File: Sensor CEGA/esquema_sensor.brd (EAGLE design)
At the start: 69.8 x 73.3 mm, 11 parts

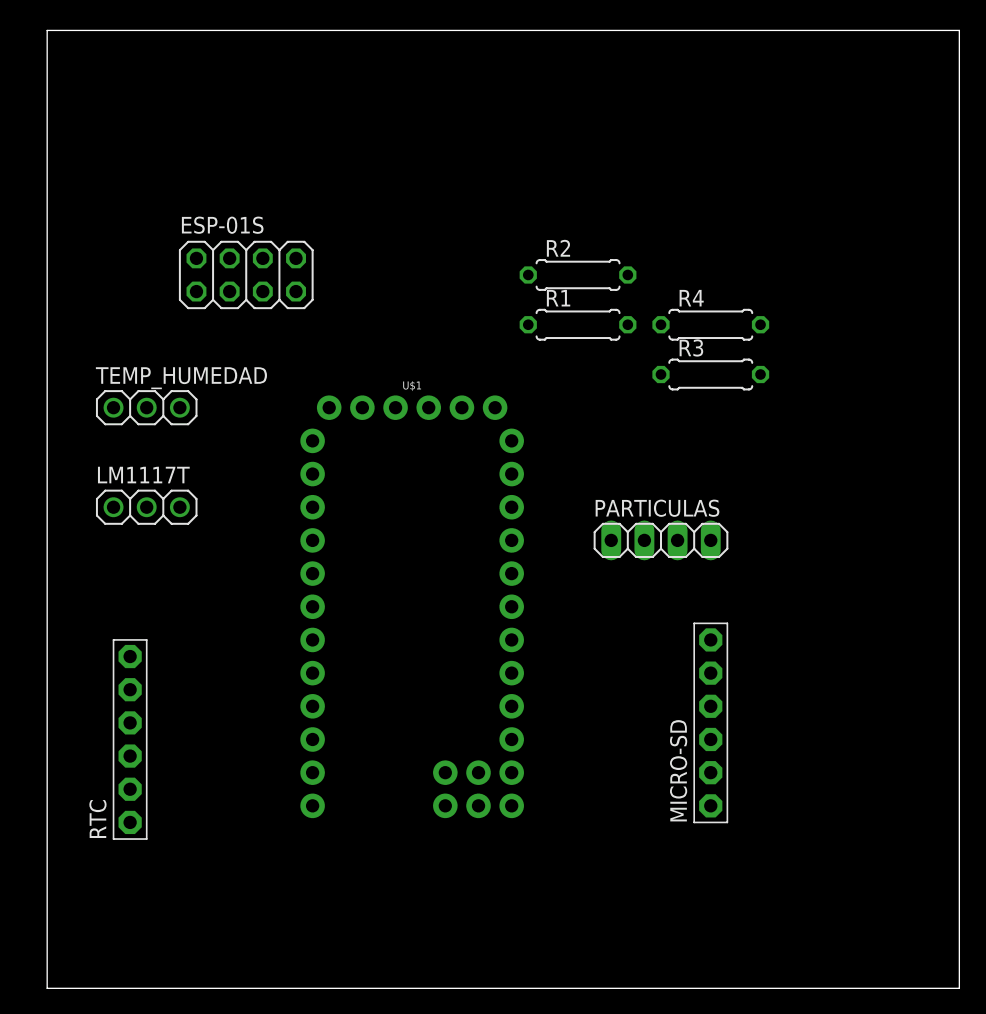
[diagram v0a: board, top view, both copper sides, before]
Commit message: versión 1.0 del sensor en PCB
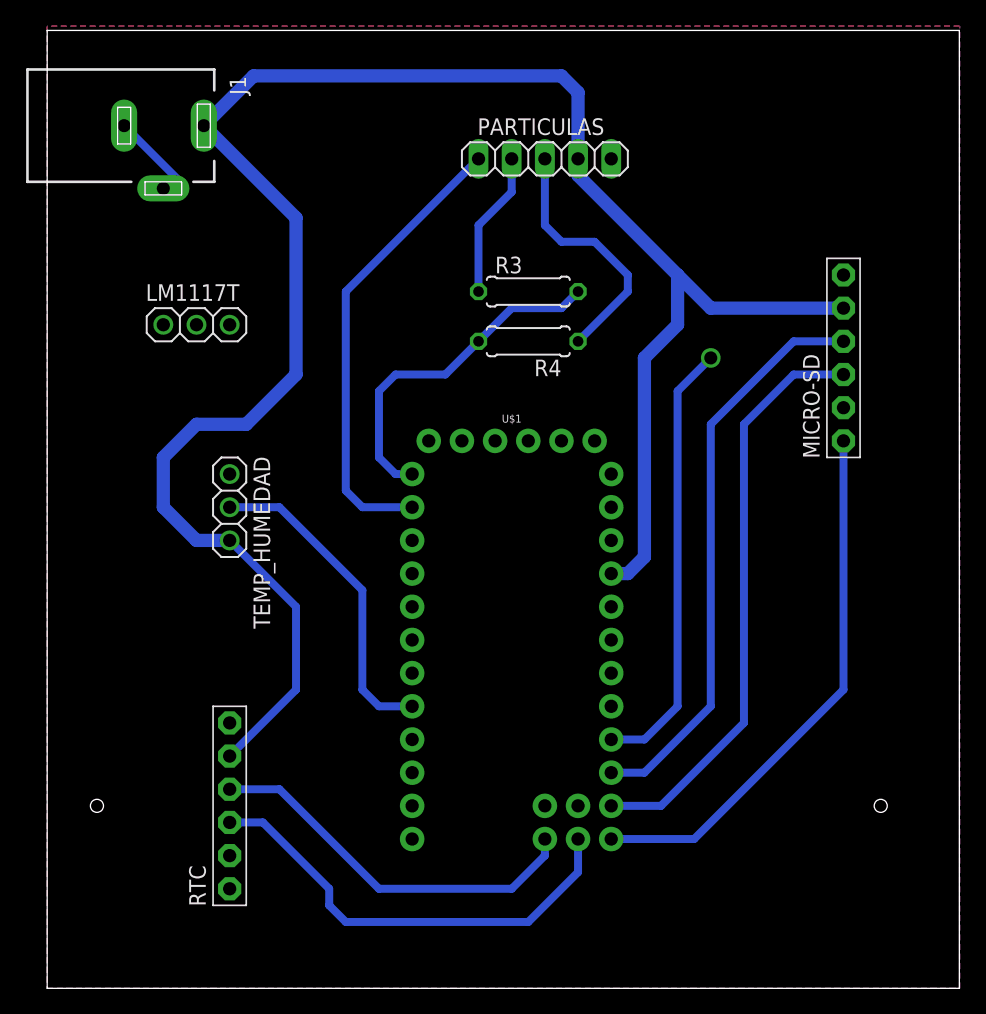
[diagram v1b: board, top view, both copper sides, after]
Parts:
- removed ESP-01S: (no value), pinhead:2X04
- removed R1, R2: (no value), resistor:0207/7
- added J1: DCJ0202, con-jack:DCJ0202
- PARTICULAS: device pinhead:1X04 -> pinhead:1X05
- moved PARTICULAS 30.5 mm to (38.1, 63.5)
- moved MICRO-SD 29.7 mm to (61.0, 48.3)
- moved R3 15.3 mm to (36.8, 53.3)
- moved LM1117T 14.5 mm to (11.4, 50.8)
- moved R4 14.0 mm to (36.8, 49.5), turned to 180 degrees
- moved TEMP_HUMEDAD 9.92 mm to (14.0, 36.8), turned to 270 degrees
- moved RTC 9.16 mm to (14.0, 14.0)
- moved U$1 8.03 mm to (35.6, 26.7)
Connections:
- removed net GND: U$1.23
- removed net N$4: ESP-01S.2, R1.2, R2.2
- net +3V3: no longer ESP-01S.1, ESP-01S.5
- net +5V: now also J1.1
- net GNDA: now also J1.2, J1.3, U$1.23; no longer ESP-01S.8, R2.1
- net N$1: no longer R1.1
- net N$3: no longer ESP-01S.7
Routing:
- net +5V: track 0.00 -> 161.7 mm
- net N$11: track 0.00 -> 44.8 mm
- net N$10: track 0.00 -> 44.1 mm
- net N$13: track 0.00 -> 41.6 mm
- net N$5: track 0.00 -> 35.2 mm
- net A5: track 0.00 -> 34.7 mm
- net N$12: track 0.00 -> 33.9 mm, vias 0 -> 1
- net A4: track 0.00 -> 29.6 mm
- net GNDA: track 0.00 -> 26.8 mm
- net N$6: track 0.00 -> 26.5 mm
- net N$8: track 0.00 -> 24.7 mm
- net N$7: track 0.00 -> 11.2 mm
- added copper zone on layer 1, net GNDA
- added copper zone on layer 16, net GNDA

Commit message: actualizado sensor cega y usain bot
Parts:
- removed LM1117T: (no value), adafruit:1X03
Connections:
- removed net +3V3: LM1117T.2
- removed net N$1: U$1.6
- removed net N$3: U$1.5
- removed net N$7: PARTICULAS.2, R3.1
- new net N$2: PARTICULAS.2, R3.2, R4.2
- net +5V: no longer LM1117T.3
- net GNDA: no longer LM1117T.1
- net N$6: now also R3.1; no longer R3.2, R4.2
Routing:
- net N$6: track 26.5 -> 13.8 mm
- net N$7: track 11.2 -> 0.00 mm
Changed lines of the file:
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@@
 </autorouter>
 <elements>
-<element name="LM1117T" library="adafruit" library_urn="urn:adsk.eagle:library:420" package="1X03" value="" x="11.43" y="50.8" smashed="yes">
-<attribute name="NAME" x="7.5438" y="52.6288" size="1.27" layer="25" ratio="10"/>
-<attribute name="VALUE" x="7.62" y="47.625" size="1.27" layer="27"/>
-</element>
 <element name="MICRO-SD" library="adafruit" library_urn="urn:adsk.eagle:library:420" package="1X06-BIG" value="" x="60.96" y="48.26" smashed="yes" rot="R90">
 <attribute name="NAME" x="59.1312" y="40.5638" size="1.27" layer="25" ratio="10" rot="R90"/>
@@
 <contactref element="U$1" pad="24"/>
 </signal>
-<signal name="N$3">
-<contactref element="U$1" pad="5"/>
-</signal>
 <signal name="N$8">
 <contactref element="TEMP_HUMEDAD" pad="2"/>
@@
 <wire x1="25.4" y1="21.59" x2="27.94" y2="21.59" width="0.6096" layer="16"/>
 </signal>
-<signal name="+3V3">
-<contactref element="LM1117T" pad="2"/>
-</signal>
 <signal name="GNDA">
 <contactref element="TEMP_HUMEDAD" pad="1"/>
@@
 <contactref element="RTC" pad="6"/>
 <contactref element="MICRO-SD" pad="6"/>
-<contactref element="LM1117T" pad="1"/>
 <contactref element="U$1" pad="4"/>
 <wire x1="38.1" y1="63.5" x2="38.1" y2="58.42" width="0.6096" layer="16"/>
@@
 <contactref element="RTC" pad="5"/>
 <contactref element="MICRO-SD" pad="5"/>
-<contactref element="LM1117T" pad="3"/>
 <contactref element="U$1" pad="21"/>
 <contactref element="J1" pad="1"/>
@@
 <wire x1="44.45" y1="31.75" x2="43.18" y2="31.75" width="1.016" layer="16"/>
 <wire x1="45.72" y1="48.26" x2="45.72" y2="33.02" width="1.016" layer="16"/>
-<wire x1="19.05" y1="46.99" x2="13.97" y2="50.8" width="0" layer="19" extent="16-16"/>
-</signal>
-<signal name="N$1">
-<contactref element="U$1" pad="6"/>
 </signal>
 <signal name="N$5">
@@
 </signal>
 <signal name="N$6">
-<contactref element="R3" pad="2"/>
-<contactref element="R4" pad="2"/>
 <contactref element="U$1" pad="1"/>
-<wire x1="40.64" y1="53.34" x2="39.37" y2="52.07" width="0.6096" layer="16"/>
-<wire x1="35.56" y1="52.07" x2="33.02" y2="49.53" width="0.6096" layer="16"/>
-<wire x1="39.37" y1="52.07" x2="35.56" y2="52.07" width="0.6096" layer="16"/>
-<wire x1="33.02" y1="49.53" x2="30.48" y2="46.99" width="0.6096" layer="16"/>
 <wire x1="30.48" y1="46.99" x2="26.67" y2="46.99" width="0.6096" layer="16"/>
 <wire x1="26.67" y1="46.99" x2="25.4" y2="45.72" width="0.6096" layer="16"/>
@@
 <wire x1="25.4" y1="40.64" x2="26.67" y2="39.37" width="0.6096" layer="16"/>
 <wire x1="26.67" y1="39.37" x2="27.94" y2="39.37" width="0.6096" layer="16"/>
-</signal>
-<signal name="N$7">
 <contactref element="R3" pad="1"/>
-<contactref element="PARTICULAS" pad="2"/>
-<wire x1="33.02" y1="53.34" x2="33.02" y2="58.42" width="0.6096" layer="16"/>
-<wire x1="33.02" y1="58.42" x2="35.56" y2="60.96" width="0.6096" layer="16"/>
-<wire x1="35.56" y1="60.96" x2="35.56" y2="63.5" width="0.6096" layer="16"/>
+<wire x1="30.48" y1="46.99" x2="33.02" y2="53.34" width="0" layer="19" extent="16-16"/>
 </signal>
 <signal name="N$10">
@@
 <wire x1="16.51" y1="12.7" x2="21.59" y2="7.62" width="0.6096" layer="16"/>
 </signal>
+<signal name="N$2">
+<contactref element="R3" pad="2"/>
+<contactref element="R4" pad="2"/>
+<contactref element="PARTICULAS" pad="2"/>
+<wire x1="40.64" y1="53.34" x2="35.56" y2="63.5" width="0" layer="19" extent="1-1"/>
+<wire x1="33.02" y1="49.53" x2="40.64" y2="53.34" width="0" layer="19" extent="1-1"/>
+</signal>
 </signals>

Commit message: last version and fotos
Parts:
- removed J1: DCJ0202, con-jack:DCJ0202
- removed MICRO-SD: (no value), adafruit:1X06-BIG
- added J2: (no value), SparkFun-Connectors:SCREWTERMINAL-5MM-2
- added SD_READER: MICRO_SD_READER, fablab_uchile:MICRO_SD_READER
- R3: value (none) -> 100
- R4: value (none) -> 200
- RTC: value (none) -> DS3231_RTC; device adafruit:1X06-BIG -> fablab_uchile:DS3231_RTC
- U$1: value PRO_MINI_CEGA -> PRO_MINI_CEGAPRO_MINI_MOD; device fablab_uchile:ARDUINO_PRO_MINI -> fablab_uchile:ARDUINO_PRO_MINI_MOD
- moved TEMP_HUMEDAD 47.7 mm to (55.9, 59.7), turned to 0 degrees
- moved R3 19.0 mm to (17.8, 53.3), turned to 90 degrees
- moved U$1 18.3 mm to (20.3, 36.8), turned to 90 degrees
- moved RTC 14.0 mm to (27.9, 12.7), turned to 270 degrees
- moved R4 12.0 mm to (26.7, 55.9)
- moved PARTICULAS 2.84 mm to (35.6, 62.2)
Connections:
- net N$5 renamed D1
- net N$6 renamed D0
- net N$8 renamed D5
- removed net GNDA: J1.2, J1.3, MICRO-SD.6, PARTICULAS.3, R4.1, RTC.6, TEMP_HUMEDAD.1, U$1.23, U$1.4
- removed net N$10: MICRO-SD.4, U$1.15
- removed net N$11: MICRO-SD.3, U$1.14
- removed net N$12: MICRO-SD.2, U$1.16
- removed net N$13: MICRO-SD.1, U$1.13
- new net D10: SD_READER.CS, U$1.13
- new net D11: SD_READER.MOSI, U$1.14
- new net D12: SD_READER.MISO, U$1.15
- new net D13: SD_READER.SCK, U$1.16
- new net GND: J2.1, PARTICULAS.3, R4.1, RTC.GND, SD_READER.GND, TEMP_HUMEDAD.1, U$1.23, U$1.4
- net +5V: now also J2.2, RTC.VCC, SD_READER.VCC; no longer J1.1, MICRO-SD.5, RTC.5
- net A4: now also RTC.SDA; no longer RTC.4
- net A5: now also RTC.SCL; no longer RTC.3
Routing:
- net GND: track 0.00 -> 104.6 mm
- net D5: track 24.7 -> 112.0 mm
- net D13: track 0.00 -> 49.0 mm, vias 0 -> 2
- net N$11: track 44.8 -> 0.00 mm
- net N$10: track 44.1 -> 0.00 mm
- net D1: track 35.2 -> 78.9 mm
- net N$13: track 41.6 -> 0.00 mm
- net D11: track 0.00 -> 36.0 mm, vias 0 -> 3
- net D10: track 0.00 -> 34.5 mm, vias 0 -> 2
- net N$12: track 33.9 -> 0.00 mm, vias 1 -> 0
- net D12: track 0.00 -> 33.9 mm, vias 0 -> 2
- net GNDA: track 26.8 -> 0.00 mm
- net D0: track 13.8 -> 40.2 mm
- net N$2: track 0.00 -> 21.9 mm
- net +5V: track 161.7 -> 150.7 mm
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- added copper zone on layer 1, net GND
- added copper zone on layer 16, net GND
- removed copper zone on layer 1, net GNDA
- removed copper zone on layer 16, net GNDA
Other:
- board size 69.8 x 73.3 mm -> 68.6 x 69.5 mm
